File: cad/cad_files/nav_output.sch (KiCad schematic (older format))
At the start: 5 parts

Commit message: ERC clearing
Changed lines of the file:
@@
-EESchema Schematic File Version 2  date Wed 03 Dec 2014 05:36:52 PM HST
+EESchema Schematic File Version 2  date Wed 03 Dec 2014 05:46:12 PM HST
 LIBS:local_parts
 LIBS:power
@@
 Connection ~ 4200 3400
 Wire Wire Line
-	3700 3400 4200 3400
-Wire Wire Line
-	4200 3400 4700 3400
+	3700 3400 4700 3400
 Connection ~ 5000 4800
 Wire Wire Line
@@
 	5800 3400 5300 3400
 Wire Wire Line
-	4000 4050 4300 4050
+	4300 4050 4000 4050
 Wire Wire Line
 	4300 4250 4200 4250
@@
 	4300 3750 4200 3750
 Wire Wire Line
-	4200 4250 4200 3750
-Wire Wire Line
-	4200 3750 4200 3400
+	4200 4250 4200 3400
 Connection ~ 4200 3750
 Wire Wire Line
@@
 	6600 4450 6600 4800
 Wire Wire Line
-	6600 4800 6300 4800
-Wire Wire Line
-	6300 4800 5000 4800
-Wire Wire Line
-	5000 4800 4000 4800
-Wire Wire Line
-	4000 4800 3800 4800
+	6600 4800 3800 4800
 Connection ~ 6300 4800
 Wire Wire Line
@@
 Connection ~ 4000 4800
 Wire Wire Line
-	4000 3600 4000 4050
-Wire Wire Line
-	4000 4050 4000 4150
+	4000 3600 4000 4150
 Connection ~ 4000 4050
 Text HLabel 3700 3600 0    60   Input ~ 0

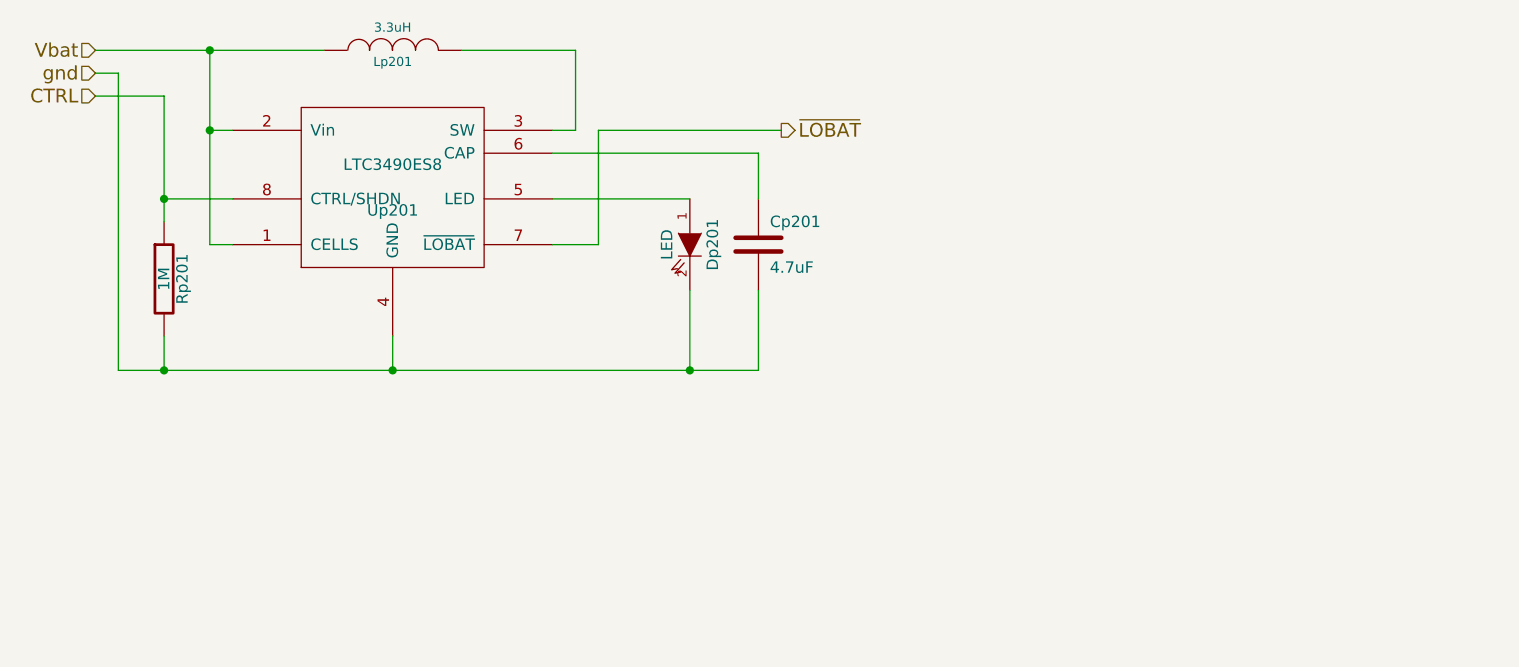
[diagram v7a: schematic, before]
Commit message: Prep for layout
add footprints, refine design
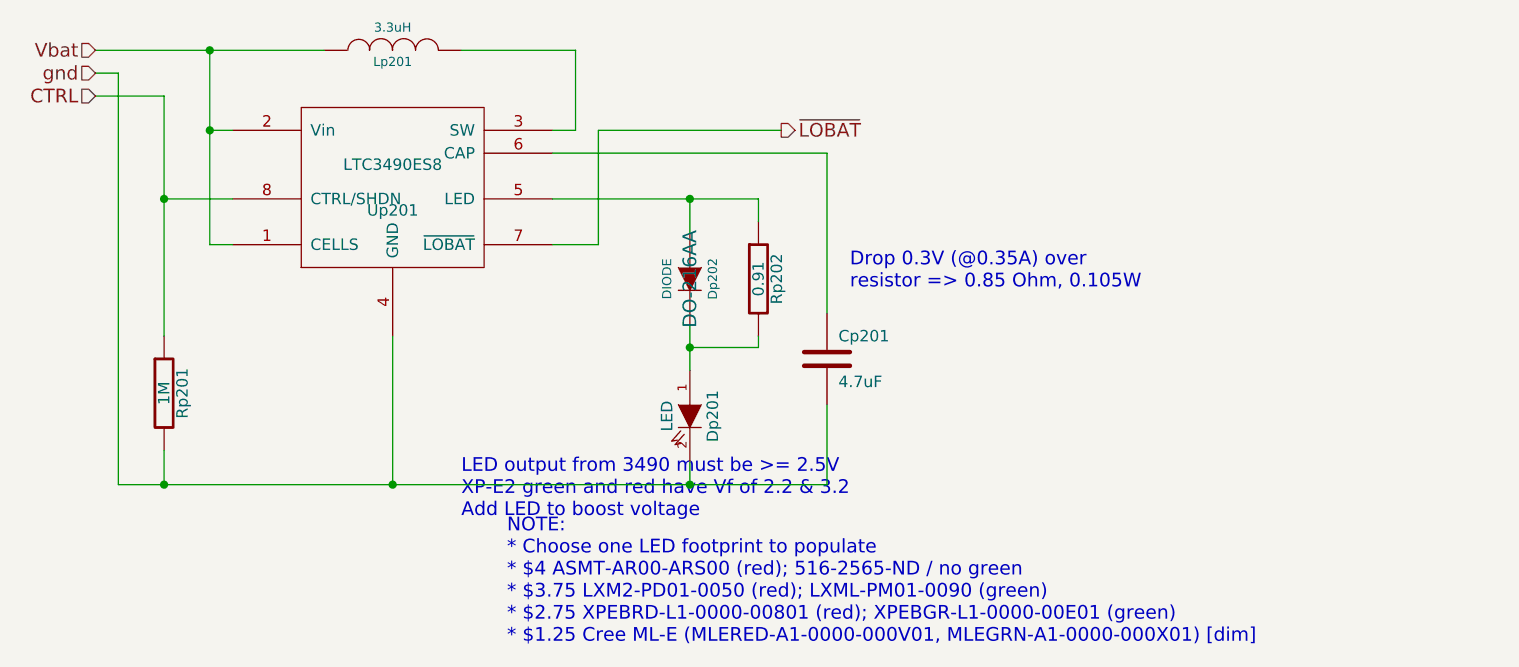
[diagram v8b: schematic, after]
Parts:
- added Dp202: DIODE, DO-216AA, symbol DIODE
- added Rp202: 0.91, SM0805, symbol R
- Cp201: footprint (none) -> SM0805; digikey (none) -> 445-1421-1-ND
- Dp201: footprint (none) -> XP-E2; digikey (none) -> XPEBRD-L1-0000-00801CT-ND
- Lp201: footprint (none) -> SLF7045; digikey (none) -> 445-2023-1-ND
- Rp201: footprint (none) -> SM0805; digikey (none) -> P1.00MCCT-ND
- Up201: footprint MODULE -> SOIC_8n; digikey (none) -> LTC3490ES8#PBF-ND
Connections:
- net at Up201.5 (LED): now also Dp202.1 (A), Rp202.1; no longer Dp201.1 (A)
- new net: Dp201.1 (A), Dp202.2 (K), Rp202.2
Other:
- note added: "Drop 0.3V (@0.35A) over \nresistor => 0.85 Ohm, 0.105W"
- note added: "LED output from 3490 must be >= 2.5V\nXP-E2 green and red have Vf of 2.2 & 3.2\nAdd LED to boost voltage"
- note added: "NOTE:\n* Choose one LED footprint to populate\n* $4 ASMT-AR00-ARS00 (red); 516-2565-ND / no green\n* $3.75 LXM2-PD01-0050 (red); LXML-PM01-0090 (green)\n* $2.75 XPEBRD-L1-0000-00801 (red); XPEBGR-L1-0000-00E01 (green)\n* $1.25 Cree ML-E (MLERED-A1-0000-000V01, MLEGRN-A1-0000-000X01) [dim]"
- moved on the sheet: Cp201, Dp201, Rp201
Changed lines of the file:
@@
-EESchema Schematic File Version 2  date Wed 03 Dec 2014 05:46:12 PM HST
+EESchema Schematic File Version 2  date Sun 07 Dec 2014 02:35:16 AM HST
 LIBS:local_parts
 LIBS:power
@@
 Sheet 4 4
 Title "LED Driver"
-Date "4 dec 2014"
+Date "7 dec 2014"
 Rev ""
 Comp ""
@@
 Comment4 ""
 $EndDescr
+Text Notes 7000 4450 0    60   ~ 0
+Drop 0.3V (@0.35A) over \nresistor => 0.85 Ohm, 0.105W
+Connection ~ 6300 4050
+Wire Wire Line
+	6600 4050 6600 4150
+Wire Wire Line
+	5700 4050 6300 4050
+Wire Wire Line
+	6300 4050 6600 4050
+Wire Wire Line
+	6300 4600 6300 4700
+Wire Wire Line
+	6300 4700 6300 4800
 Wire Wire Line
 	5700 4250 5900 4250
@@
 Connection ~ 4200 3400
 Wire Wire Line
-	3700 3400 4700 3400
-Connection ~ 5000 4800
-Wire Wire Line
-	6300 4450 6300 4800
-Wire Wire Line
-	5700 4050 6300 4050
+	3700 3400 4200 3400
+Wire Wire Line
+	4200 3400 4700 3400
+Connection ~ 5000 5300
+Wire Wire Line
+	6300 5200 6300 5300
 Wire Wire Line
 	5700 3750 5800 3750
@@
 	4300 3750 4200 3750
 Wire Wire Line
-	4200 4250 4200 3400
+	4200 4250 4200 3750
+Wire Wire Line
+	4200 3750 4200 3400
 Connection ~ 4200 3750
 Wire Wire Line
-	5700 3850 6600 3850
-Wire Wire Line
-	6600 3850 6600 4050
-Wire Wire Line
-	5000 4800 5000 4650
-Wire Wire Line
-	4000 4800 4000 4650
-Wire Wire Line
-	6600 4450 6600 4800
-Wire Wire Line
-	6600 4800 3800 4800
-Connection ~ 6300 4800
+	5700 3850 6900 3850
+Wire Wire Line
+	6900 3850 6900 4550
+Wire Wire Line
+	4000 5300 4000 5150
+Wire Wire Line
+	6900 4950 6900 5300
+Wire Wire Line
+	6900 5300 6300 5300
+Wire Wire Line
+	6300 5300 5000 5300
+Wire Wire Line
+	5000 5300 4000 5300
+Wire Wire Line
+	4000 5300 3800 5300
+Connection ~ 6300 5300
 Wire Wire Line
 	3700 3500 3800 3500
 Wire Wire Line
-	3800 3500 3800 4800
-Connection ~ 4000 4800
-Wire Wire Line
-	4000 3600 4000 4150
+	3800 3500 3800 5300
+Connection ~ 4000 5300
+Wire Wire Line
+	4000 3600 4000 4050
+Wire Wire Line
+	4000 4050 4000 4650
 Connection ~ 4000 4050
+Wire Wire Line
+	6300 4050 6300 4200
+Wire Wire Line
+	5000 5300 5000 4650
+Wire Wire Line
+	6300 4700 6600 4700
+Wire Wire Line
+	6600 4700 6600 4650
+Connection ~ 6300 4700
+$Comp
+L R Rp202
+U 1 1 54813C92
+P 6600 4400
+F 0 "Rp202" V 6680 4400 50  0000 C CNN
+F 1 "0.91" V 6600 4400 50  0000 C CNN
+F 2 "SM0805" H 6600 4400 60  0001 C CNN
+F 4 "CRM0805-FX-R910ELF" V 6600 4400 60  0001 C CNN "digikey"
+	1    6600 4400
+	1    0    0    -1
+$EndComp
+Text Notes 5300 5450 0    60   ~ 0
+LED output from 3490 must be >= 2.5V\nXP-E2 green and red have Vf of 2.2 & 3.2\nAdd LED to boost voltage
+$Comp
+L DIODE Dp202
+U 1 1 548139A3
+P 6300 4400
+F 0 "Dp202" H 6300 4500 40  0000 C CNN
+F 1 "DIODE" H 6300 4300 40  0000 C CNN
+F 2 "DO-216AA" H 6300 4400 60  0000 C CNN
+F 4 "MBRM120ET3GOSCT-ND" H 6300 4400 60  0001 C CNN "digikey"
+	1    6300 4400
+	0    1    1    0
+$EndComp
+Text Notes 5500 6000 0    60   ~ 0
+NOTE:\n* Choose one LED footprint to populate\n* $4 ASMT-AR00-ARS00 (red); 516-2565-ND / no green\n* $3.75 LXM2-PD01-0050 (red); LXML-PM01-0090 (green)\n* $2.75 XPEBRD-L1-0000-00801 (red); XPEBGR-L1-0000-00E01 (green)\n* $1.25 Cree ML-E (MLERED-A1-0000-000V01, MLEGRN-A1-0000-000X01) [dim]
 Text HLabel 3700 3600 0    60   Input ~ 0
 CTRL
@@
 L LED Dp201
 U 1 1 53D0E361
-P 6300 4250
-F 0 "Dp201" H 6300 4350 50  0000 C CNN
-F 1 "LED" H 6300 4150 50  0000 C CNN
-	1    6300 4250
+P 6300 5000
+F 0 "Dp201" H 6300 5100 50  0000 C CNN
+F 1 "LED" H 6300 4900 50  0000 C CNN
+F 2 "XP-E2" H 6300 5000 60  0001 C CNN
+F 4 "XPEBRD-L1-0000-00801CT-ND" H 6300 5000 60  0001 C CNN "digikey"
+	1    6300 5000
 	0    1    1    0
 $EndComp
@@
 F 0 "Lp201" V 4950 3400 40  0000 C CNN
 F 1 "3.3uH" V 5100 3400 40  0000 C CNN
+F 2 "SLF7045" H 5000 3400 60  0001 C CNN
+F 4 "445-2023-1-ND" V 5000 3400 60  0001 C CNN "digikey"
 	1    5000 3400
 	0    -1   -1   0
@@
 L C Cp201
 U 1 1 53D0E16B
-P 6600 4250
-F 0 "Cp201" H 6650 4350 50  0000 L CNN
-F 1 "4.7uF" H 6650 4150 50  0000 L CNN
-	1    6600 4250
+P 6900 4750
+F 0 "Cp201" H 6950 4850 50  0000 L CNN
+F 1 "4.7uF" H 6950 4650 50  0000 L CNN
+F 2 "SM0805" H 6900 4750 60  0001 C CNN
+F 4 "445-1421-1-ND" H 6900 4750 60  0001 C CNN "digikey"
+	1    6900 4750
 	1    0    0    -1
 $EndComp
@@
 L R Rp201
 U 1 1 53D0E165
-P 4000 4400
-F 0 "Rp201" V 4080 4400 50  0000 C CNN
-F 1 "1M" V 4000 4400 50  0000 C CNN
-	1    4000 4400
+P 4000 4900
+F 0 "Rp201" V 4080 4900 50  0000 C CNN
+F 1 "1M" V 4000 4900 50  0000 C CNN
+F 2 "SM0805" H 4000 4900 60  0001 C CNN
+F 4 "P1.00MCCT-ND" V 4000 4900 60  0001 C CNN "digikey"
+	1    4000 4900
 	1    0    0    -1
 $EndComp
@@
 F 0 "Up201" H 5000 3900 50  0000 C CNN
 F 1 "LTC3490ES8" H 5000 4100 50  0000 C CNN
-F 2 "MODULE" H 5000 4000 50  0001 C CNN
+F 2 "SOIC_8n" H 5000 4000 50  0001 C CNN
 F 3 "DOCUMENTATION" H 5000 4000 50  0001 C CNN
+F 4 "LTC3490ES8#PBF-ND" H 5000 4000 60  0001 C CNN "digikey"
 	1    5000 4000
 	1    0    0    -1
